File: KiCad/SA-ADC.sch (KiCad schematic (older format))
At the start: 0 parts

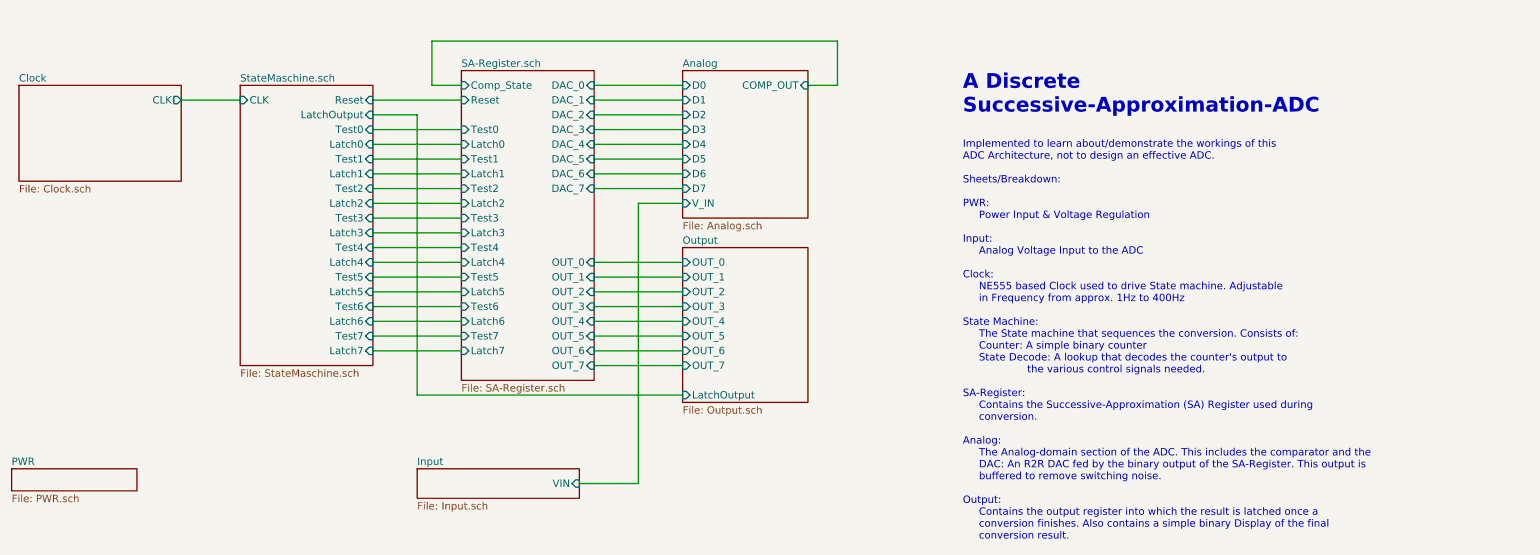
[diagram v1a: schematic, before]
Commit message: Schematic Update First Draft, ERC Passed
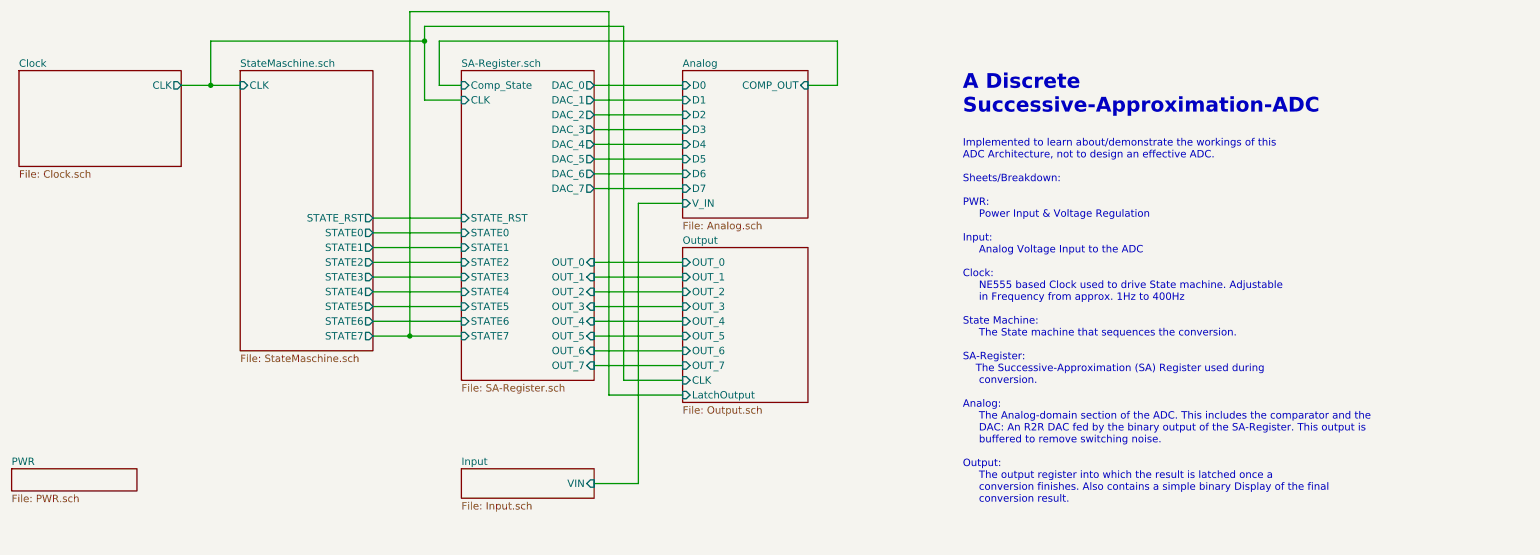
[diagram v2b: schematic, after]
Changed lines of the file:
@@
 $Descr A4 11693 8268
 encoding utf-8
-Sheet 1 11
+Sheet 1 9
 Title "Schilk_SA-ADC"
 Date ""
@@
 Comment4 ""
 $EndDescr
-$Sheet
-S 2450 1100 900  1900
-U 5E356A03
-F0 "StateMaschine.sch" 50
-F1 "StateMaschine.sch" 50
-F2 "CLK" I L 2450 1200 50
-F3 "Reset" I R 3350 1200 50
-F4 "LatchOutput" I R 3350 1300 50
-F5 "Test0" I R 3350 1400 50
-F6 "Test1" I R 3350 1600 50
-F7 "Test2" I R 3350 1800 50
-F8 "Test3" I R 3350 2000 50
-F9 "Test4" I R 3350 2200 50
-F10 "Test5" I R 3350 2400 50
-F11 "Test6" I R 3350 2600 50
-F12 "Test7" I R 3350 2800 50
-F13 "Latch0" I R 3350 1500 50
-F14 "Latch1" I R 3350 1700 50
-F15 "Latch2" I R 3350 1900 50
-F16 "Latch3" I R 3350 2100 50
-F17 "Latch4" I R 3350 2300 50
-F18 "Latch5" I R 3350 2500 50
-F19 "Latch6" I R 3350 2700 50
-F20 "Latch7" I R 3350 2900 50
-$EndSheet
 $Sheet
 S 5450 1000 850  1000
@@
 $EndSheet
 Wire Wire Line
-	2450 1200 2050 1200
+	2450 1100 2250 1100
 $Sheet
 S 3950 1000 900  2100
@@
 F0 "SA-Register.sch" 50
 F1 "SA-Register.sch" 50
-F2 "Reset" I L 3950 1200 50
-F3 "Test0" I L 3950 1400 50
-F4 "Test1" I L 3950 1600 50
-F5 "Test2" I L 3950 1800 50
-F6 "Test3" I L 3950 2000 50
-F7 "Test4" I L 3950 2200 50
-F8 "Test5" I L 3950 2400 50
-F9 "Test6" I L 3950 2600 50
-F10 "Test7" I L 3950 2800 50
-F11 "Latch0" I L 3950 1500 50
-F12 "Latch1" I L 3950 1700 50
-F13 "Latch2" I L 3950 1900 50
-F14 "Latch3" I L 3950 2100 50
-F15 "Latch4" I L 3950 2300 50
-F16 "Latch5" I L 3950 2500 50
-F17 "Latch6" I L 3950 2700 50
-F18 "Latch7" I L 3950 2900 50
-F19 "DAC_0" I R 4850 1100 50
-F20 "DAC_1" I R 4850 1200 50
-F21 "DAC_2" I R 4850 1300 50
-F22 "DAC_3" I R 4850 1400 50
-F23 "DAC_4" I R 4850 1500 50
-F24 "DAC_5" I R 4850 1600 50
-F25 "DAC_6" I R 4850 1700 50
-F26 "DAC_7" I R 4850 1800 50
-F27 "OUT_0" I R 4850 2300 50
-F28 "OUT_1" I R 4850 2400 50
-F29 "OUT_2" I R 4850 2500 50
-F30 "OUT_3" I R 4850 2600 50
-F31 "OUT_4" I R 4850 2700 50
-F32 "OUT_5" I R 4850 2800 50
-F33 "OUT_6" I R 4850 2900 50
-F34 "OUT_7" I R 4850 3000 50
-F35 "Comp_State" I L 3950 1100 50
-$EndSheet
-Wire Wire Line
-	3350 1200 3950 1200
-Wire Wire Line
-	3350 1400 3950 1400
-Wire Wire Line
-	3350 1500 3950 1500
-Wire Wire Line
-	3350 1600 3950 1600
-Wire Wire Line
-	3350 1700 3950 1700
-Wire Wire Line
-	3350 1800 3950 1800
-Wire Wire Line
-	3350 1900 3950 1900
-Wire Wire Line
-	3350 2000 3950 2000
-Wire Wire Line
-	3350 2100 3950 2100
-Wire Wire Line
-	3350 2200 3950 2200
-Wire Wire Line
-	3350 2300 3950 2300
-Wire Wire Line
-	3350 2400 3950 2400
-Wire Wire Line
-	3350 2500 3950 2500
-Wire Wire Line
-	3350 2600 3950 2600
-Wire Wire Line
-	3350 2700 3950 2700
-Wire Wire Line
-	3350 2800 3950 2800
-Wire Wire Line
-	3350 2900 3950 2900
+F2 "OUT_0" I R 4850 2300 50
+F3 "OUT_1" I R 4850 2400 50
+F4 "OUT_2" I R 4850 2500 50
+F5 "OUT_3" I R 4850 2600 50
+F6 "OUT_4" I R 4850 2700 50
+F7 "OUT_5" I R 4850 2800 50
+F8 "OUT_6" I R 4850 2900 50
+F9 "OUT_7" I R 4850 3000 50
+F10 "Comp_State" I L 3950 1100 50
+F11 "DAC_0" O R 4850 1100 50
+F12 "DAC_1" O R 4850 1200 50
+F13 "DAC_4" O R 4850 1500 50
+F14 "DAC_5" O R 4850 1600 50
+F15 "DAC_6" O R 4850 1700 50
+F16 "DAC_3" O R 4850 1400 50
+F17 "DAC_2" O R 4850 1300 50
+F18 "STATE0" I L 3950 2100 50
+F19 "STATE1" I L 3950 2200 50
+F20 "STATE2" I L 3950 2300 50
+F21 "STATE3" I L 3950 2400 50
+F22 "STATE4" I L 3950 2500 50
+F23 "STATE5" I L 3950 2600 50
+F24 "STATE6" I L 3950 2700 50
+F25 "STATE7" I L 3950 2800 50
+F26 "CLK" I L 3950 1200 50
+F27 "STATE_RST" I L 3950 2000 50
+F28 "DAC_7" O R 4850 1800 50
+$EndSheet
 Wire Wire Line
 	4850 1100 5450 1100
@@
 Wire Wire Line
 	6500 1100 6500 800
-Wire Wire Line
-	6500 800  3750 800
-Wire Wire Line
-	3750 800  3750 1100
-Wire Wire Line
-	3750 1100 3950 1100
 Wire Wire Line
 	5150 1900 5450 1900
@@
 F9 "OUT_7" I L 5450 3000 50
 F10 "LatchOutput" I L 5450 3200 50
+F11 "CLK" I L 5450 3100 50
 $EndSheet
 Wire Wire Line
@@
 Wire Wire Line
 	4850 3000 5450 3000
-$Sheet
-S 3650 3700 1100 200
-U 5E371FE4
-F0 "Input" 50
-F1 "Input.sch" 50
-F2 "VIN" I R 4750 3800 50
-$EndSheet
 $Sheet
 S 900  3700 850  150
@@
 Wire Wire Line
 	5150 3800 5150 1900
-Wire Wire Line
-	4750 3800 5150 3800
-$Sheet
-S 950  1100 1100 650
+$Sheet
+S 950  1000 1100 650
 U 5E356AC1
 F0 "Clock" 50
 F1 "Clock.sch" 50
-F2 "CLK" O R 2050 1200 50
-$EndSheet
-Text Notes 7350 4350 0    50   ~ 0
-Implemented to learn about/demonstrate the workings of this \nADC Architecture, not to design an effective ADC.\n\nSheets/Breakdown:\n\nPWR:\n     Power Input & Voltage Regulation\n\nInput:\n     Analog Voltage Input to the ADC\n\nClock:\n     NE555 based Clock used to drive State machine. Adjustable\n     in Frequency from approx. 1Hz to 400Hz\n\nState Machine:\n     The State machine that sequences the conversion. Consists of:\n     Counter: A simple binary counter \n     State Decode: A lookup that decodes the counter's output to \n                    the various control signals needed.\n\nSA-Register:\n     Contains the Successive-Approximation (SA) Register used during      \n     conversion.\n\nAnalog:\n     The Analog-domain section of the ADC. This includes the comparator and the \n     DAC: An R2R DAC fed by the binary output of the SA-Register. This output is\n     buffered to remove switching noise. \n\nOutput:\n     Contains the output register into which the result is latched once a    \n     conversion finishes. Also contains a simple binary Display of the final \n     conversion result.\n\n\n
+F2 "CLK" O R 2050 1100 50
+$EndSheet
+Text Notes 7350 4100 0    50   ~ 0
+Implemented to learn about/demonstrate the workings of this \nADC Architecture, not to design an effective ADC.\n\nSheets/Breakdown:\n\nPWR:\n     Power Input & Voltage Regulation\n\nInput:\n     Analog Voltage Input to the ADC\n\nClock:\n     NE555 based Clock used to drive State machine. Adjustable\n     in Frequency from approx. 1Hz to 400Hz\n\nState Machine:\n     The State machine that sequences the conversion.\n\nSA-Register:\n    The Successive-Approximation (SA) Register used during      \n     conversion.\n\nAnalog:\n     The Analog-domain section of the ADC. This includes the comparator and the \n     DAC: An R2R DAC fed by the binary output of the SA-Register. This output is\n     buffered to remove switching noise. \n\nOutput:\n     The output register into which the result is latched once a    \n     conversion finishes. Also contains a simple binary Display of the final \n     conversion result.\n\n\n
 Text Notes 7350 1300 0    100  ~ 20
 A Discrete \nSuccessive-Approximation-ADC\n
-Wire Wire Line
-	3350 1300 3650 1300
-Wire Wire Line
-	3650 1300 3650 3200
-Wire Wire Line
-	3650 3200 5450 3200
+$Sheet
+S 2450 1000 900  1900
+U 5E356A03
+F0 "StateMaschine.sch" 50
+F1 "StateMaschine.sch" 50
+F2 "CLK" I L 2450 1100 50
+F3 "STATE0" O R 3350 2100 50
+F4 "STATE1" O R 3350 2200 50
+F5 "STATE2" O R 3350 2300 50
+F6 "STATE3" O R 3350 2400 50
+F7 "STATE4" O R 3350 2500 50
+F8 "STATE5" O R 3350 2600 50
+F9 "STATE6" O R 3350 2700 50
+F10 "STATE7" O R 3350 2800 50
+F11 "STATE_RST" O R 3350 2000 50
+$EndSheet
+Wire Wire Line
+	3950 1100 3800 1100
+Wire Wire Line
+	3800 1100 3800 800
+Wire Wire Line
+	3800 800  6500 800
+Wire Wire Line
+	3950 1200 3700 1200
+Wire Wire Line
+	3700 1200 3700 800
+Wire Wire Line
+	3700 800  2250 800
+Wire Wire Line
+	2250 800  2250 1100
+Connection ~ 2250 1100
+Wire Wire Line
+	2250 1100 2050 1100
+Wire Wire Line
+	3350 2000 3950 2000
+Wire Wire Line
+	3350 2100 3950 2100
+Wire Wire Line
+	3350 2200 3950 2200
+Wire Wire Line
+	3350 2300 3950 2300
+Wire Wire Line
+	3350 2400 3950 2400
+Wire Wire Line
+	3350 2500 3950 2500
+Wire Wire Line
+	3350 2600 3950 2600
+Wire Wire Line
+	3350 2700 3950 2700
+Wire Wire Line
+	3350 2800 3600 2800
+Wire Wire Line
+	5450 3100 5050 3100
+Wire Wire Line
+	5050 3100 5050 700
+Wire Wire Line
+	5050 700  3700 700
+Wire Wire Line
+	3700 700  3700 800
+Connection ~ 3700 800
+Wire Wire Line
+	5450 3200 4950 3200
+Wire Wire Line
+	4950 3200 4950 600
+Wire Wire Line
+	4950 600  3600 600
+Wire Wire Line
+	3600 600  3600 2800
+Connection ~ 3600 2800
+Wire Wire Line
+	3600 2800 3950 2800
+$Sheet
+S 3950 3700 900  200
+U 5E371FE4
+F0 "Input" 50
+F1 "Input.sch" 50
+F2 "VIN" I R 4850 3800 50
+$EndSheet
+Wire Wire Line
+	4850 3800 5150 3800
 $EndSCHEMATC

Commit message: Fixed State Numbering/Wiring Order
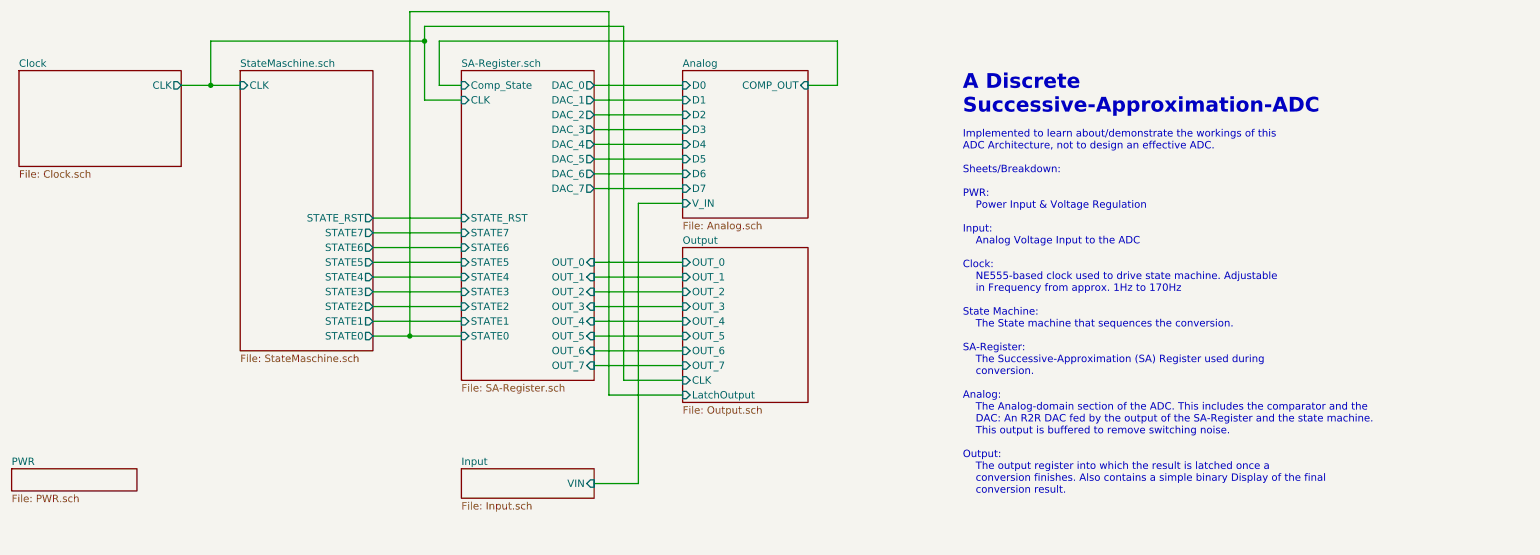
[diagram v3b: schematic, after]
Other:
- note added: "Implemented to learn about/demonstrate the workings of this \nADC Architecture, not to design an effective ADC.\n\nSheets/Breakdown:\n\nPWR:\n Power Input & Voltage Regulation\n\nInput:\n Analog Voltage Input to the ADC\n\nClock:\n NE555-based clock used to drive state machine. Adjustable\n in Frequency from approx. 1Hz to 170Hz\n\nState Machine:\n The State machine that sequences the conversion.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"
- note removed: "Implemented to learn about/demonstrate the workings of this \nADC Architecture, not to design an effective ADC.\n\nSheets/Breakdown:\n\nPWR:\n Power Input & Voltage Regulation\n\nInput:\n Analog Voltage Input to the ADC\n\nClock:\n NE555 based Clock used to drive State machine. Adjustable\n in Frequency from approx. 1Hz to 400Hz\n\nState Machine:\n The State machine that sequences the conversion.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"
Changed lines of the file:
@@
 Wire Wire Line
 	2450 1100 2250 1100
-$Sheet
-S 3950 1000 900  2100
-U 5E362800
-F0 "SA-Register.sch" 50
-F1 "SA-Register.sch" 50
-F2 "OUT_0" I R 4850 2300 50
-F3 "OUT_1" I R 4850 2400 50
-F4 "OUT_2" I R 4850 2500 50
-F5 "OUT_3" I R 4850 2600 50
-F6 "OUT_4" I R 4850 2700 50
-F7 "OUT_5" I R 4850 2800 50
-F8 "OUT_6" I R 4850 2900 50
-F9 "OUT_7" I R 4850 3000 50
-F10 "Comp_State" I L 3950 1100 50
-F11 "DAC_0" O R 4850 1100 50
-F12 "DAC_1" O R 4850 1200 50
-F13 "DAC_4" O R 4850 1500 50
-F14 "DAC_5" O R 4850 1600 50
-F15 "DAC_6" O R 4850 1700 50
-F16 "DAC_3" O R 4850 1400 50
-F17 "DAC_2" O R 4850 1300 50
-F18 "STATE0" I L 3950 2100 50
-F19 "STATE1" I L 3950 2200 50
-F20 "STATE2" I L 3950 2300 50
-F21 "STATE3" I L 3950 2400 50
-F22 "STATE4" I L 3950 2500 50
-F23 "STATE5" I L 3950 2600 50
-F24 "STATE6" I L 3950 2700 50
-F25 "STATE7" I L 3950 2800 50
-F26 "CLK" I L 3950 1200 50
-F27 "STATE_RST" I L 3950 2000 50
-F28 "DAC_7" O R 4850 1800 50
-$EndSheet
 Wire Wire Line
 	4850 1100 5450 1100
@@
 F2 "CLK" O R 2050 1100 50
 $EndSheet
-Text Notes 7350 4100 0    50   ~ 0
-Implemented to learn about/demonstrate the workings of this \nADC Architecture, not to design an effective ADC.\n\nSheets/Breakdown:\n\nPWR:\n     Power Input & Voltage Regulation\n\nInput:\n     Analog Voltage Input to the ADC\n\nClock:\n     NE555 based Clock used to drive State machine. Adjustable\n     in Frequency from approx. 1Hz to 400Hz\n\nState Machine:\n     The State machine that sequences the conversion.\n\nSA-Register:\n    The Successive-Approximation (SA) Register used during      \n     conversion.\n\nAnalog:\n     The Analog-domain section of the ADC. This includes the comparator and the \n     DAC: An R2R DAC fed by the binary output of the SA-Register. This output is\n     buffered to remove switching noise. \n\nOutput:\n     The output register into which the result is latched once a    \n     conversion finishes. Also contains a simple binary Display of the final \n     conversion result.\n\n\n
+Text Notes 7350 4200 0    50   ~ 0
+Implemented to learn about/demonstrate the workings of this \nADC Architecture, not to design an effective ADC.\n\nSheets/Breakdown:\n\nPWR:\n    Power Input & Voltage Regulation\n\nInput:\n    Analog Voltage Input to the ADC\n\nClock:\n    NE555-based clock used to drive state machine. Adjustable\n    in Frequency from approx. 1Hz to 170Hz\n\nState Machine:\n    The State machine that sequences the conversion.\n\nSA-Register:\n    The Successive-Approximation (SA) Register used during     \n    conversion.\n\nAnalog:\n    The Analog-domain section of the ADC. This includes the comparator and the \n    DAC: An R2R DAC fed by the output of the SA-Register and the state machine. \n	This output is buffered to remove switching noise. \n\nOutput:\n    The output register into which the result is latched once a    \n    conversion finishes. Also contains a simple binary Display of the final \n    conversion result.\n\n\n\n\n
 Text Notes 7350 1300 0    100  ~ 20
 A Discrete \nSuccessive-Approximation-ADC\n
@@
 F1 "StateMaschine.sch" 50
 F2 "CLK" I L 2450 1100 50
-F3 "STATE0" O R 3350 2100 50
-F4 "STATE1" O R 3350 2200 50
-F5 "STATE2" O R 3350 2300 50
-F6 "STATE3" O R 3350 2400 50
-F7 "STATE4" O R 3350 2500 50
-F8 "STATE5" O R 3350 2600 50
-F9 "STATE6" O R 3350 2700 50
-F10 "STATE7" O R 3350 2800 50
+F3 "STATE0" O R 3350 2800 50
+F4 "STATE1" O R 3350 2700 50
+F5 "STATE2" O R 3350 2600 50
+F6 "STATE3" O R 3350 2500 50
+F7 "STATE4" O R 3350 2400 50
+F8 "STATE5" O R 3350 2300 50
+F9 "STATE6" O R 3350 2200 50
+F10 "STATE7" O R 3350 2100 50
 F11 "STATE_RST" O R 3350 2000 50
 $EndSheet
@@
 Wire Wire Line
 	4850 3800 5150 3800
+$Sheet
+S 3950 1000 900  2100
+U 5E362800
+F0 "SA-Register.sch" 50
+F1 "SA-Register.sch" 50
+F2 "OUT_0" I R 4850 2300 50
+F3 "OUT_1" I R 4850 2400 50
+F4 "OUT_2" I R 4850 2500 50
+F5 "OUT_3" I R 4850 2600 50
+F6 "OUT_4" I R 4850 2700 50
+F7 "OUT_5" I R 4850 2800 50
+F8 "OUT_6" I R 4850 2900 50
+F9 "OUT_7" I R 4850 3000 50
+F10 "Comp_State" I L 3950 1100 50
+F11 "DAC_0" O R 4850 1100 50
+F12 "DAC_1" O R 4850 1200 50
+F13 "DAC_4" O R 4850 1500 50
+F14 "DAC_5" O R 4850 1600 50
+F15 "DAC_6" O R 4850 1700 50
+F16 "DAC_3" O R 4850 1400 50
+F17 "DAC_2" O R 4850 1300 50
+F18 "STATE0" I L 3950 2800 50
+F19 "STATE1" I L 3950 2700 50
+F20 "STATE2" I L 3950 2600 50
+F21 "STATE3" I L 3950 2500 50
+F22 "STATE4" I L 3950 2400 50
+F23 "STATE5" I L 3950 2300 50
+F24 "STATE6" I L 3950 2200 50
+F25 "STATE7" I L 3950 2100 50
+F26 "CLK" I L 3950 1200 50
+F27 "STATE_RST" I L 3950 2000 50
+F28 "DAC_7" O R 4850 1800 50
+$EndSheet
 $EndSCHEMATC
